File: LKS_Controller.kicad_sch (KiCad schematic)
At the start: 7 parts, among them J1 Conn_02x05_Odd_Even

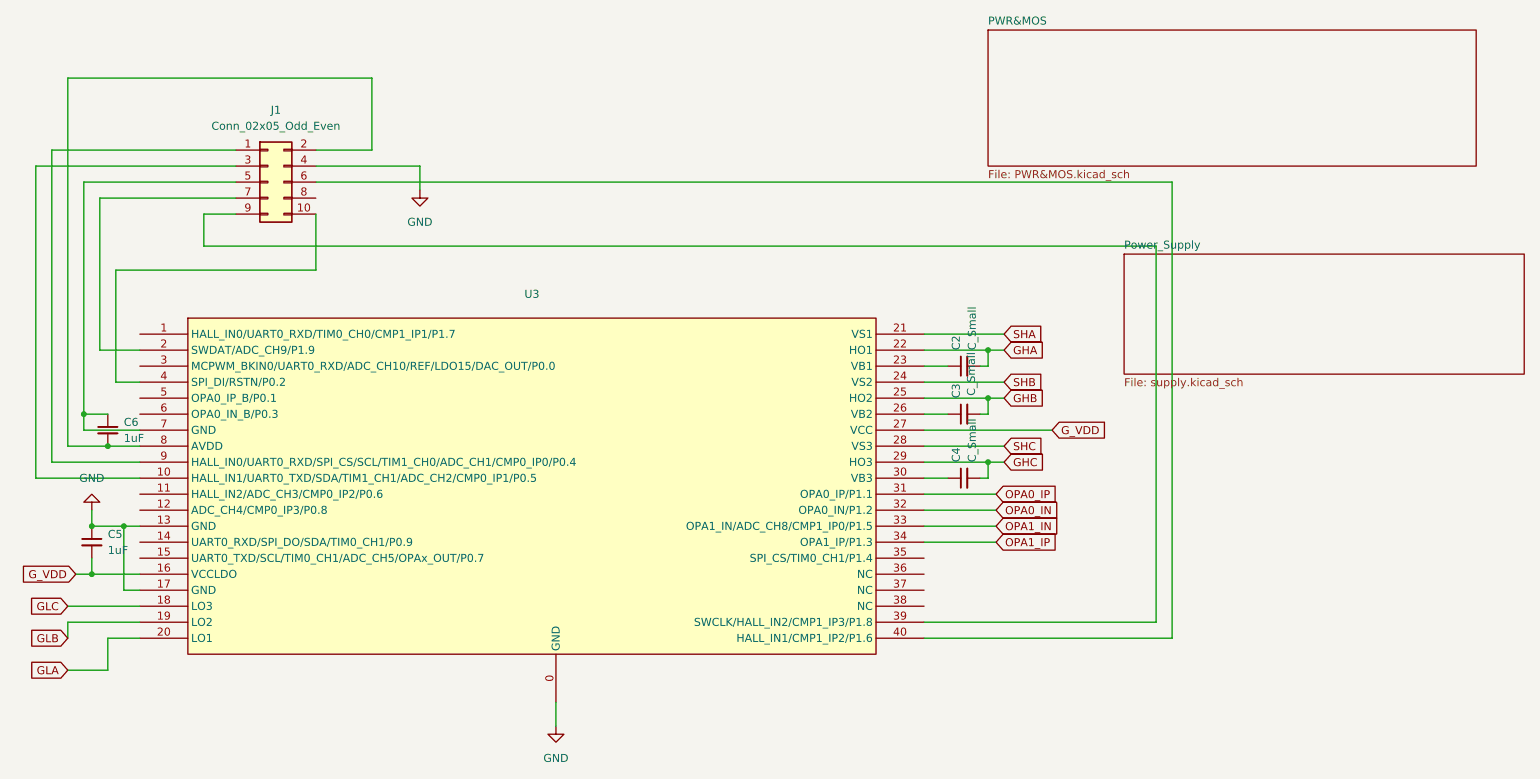
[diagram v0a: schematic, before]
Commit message: Fix ESC power, gate drive and current sensing schematics
Correct the buck converter and MCU symbols, bootstrap networks, MOSFET pulldowns and current sensing components. Migrate project libraries, synchronize PCB footprints and ground nets, and resolve ERC errors and warnings. Include LCSC BOMs and design notes; PCB routing remains incomplete.
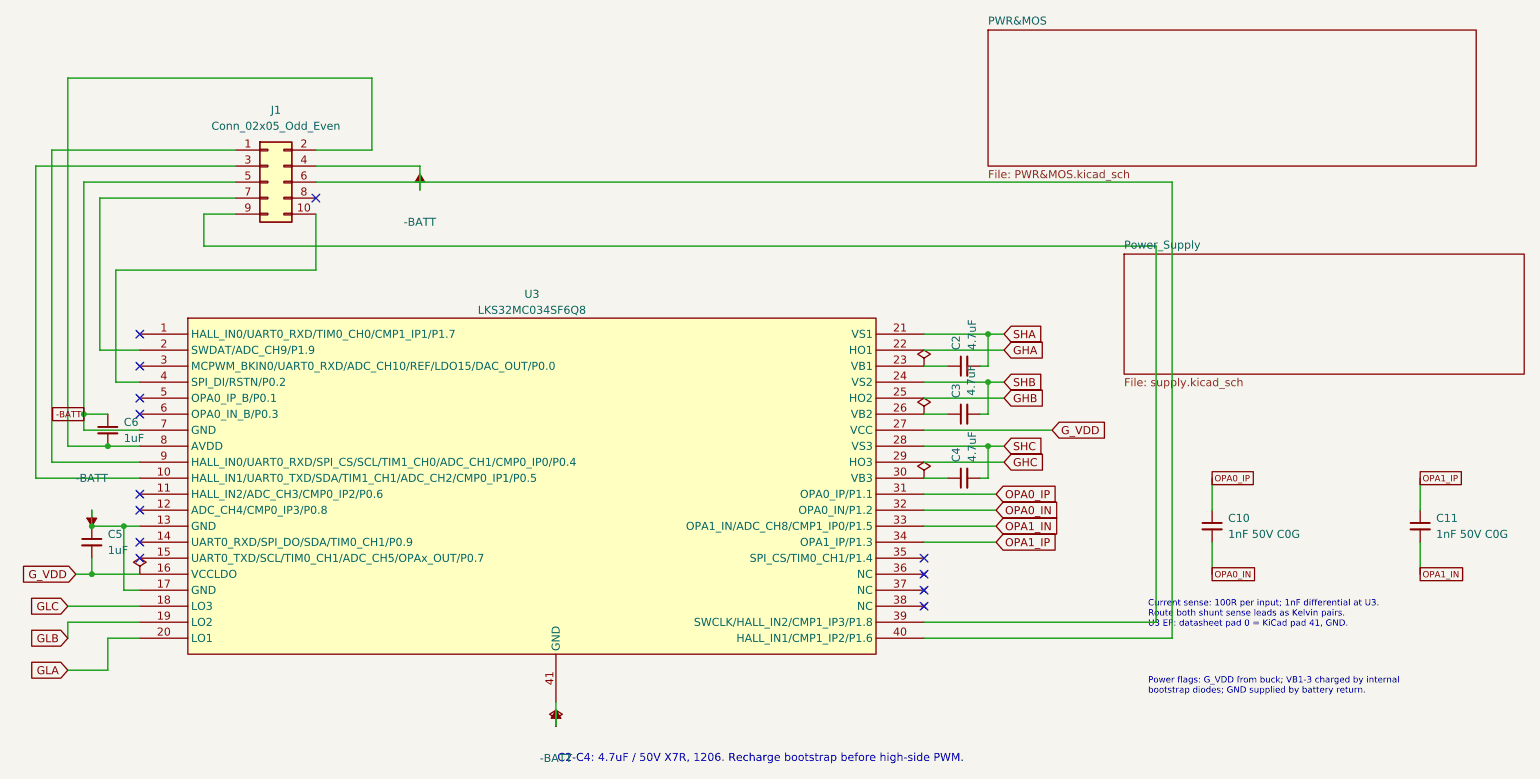
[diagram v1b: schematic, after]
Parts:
- added C10, C11: 1nF 50V C0G, Capacitor_SMD:C_0603_1608Metric_Pad1.08x0.95mm_HandSolder, symbol Device:C_Small
- C2, C3, C4: value C_Small -> 4.7uF; footprint Capacitor_SMD:C_0603_1608Metric_Pad1.08x0.95mm_HandSolder -> Capacitor_SMD:C_1206_3216Metric_Pad1.33x1.80mm_HandSolder; Dielectric (none) -> X7R; LCSC (none) -> C132170; MPN (none) -> CC1206KKX7R9BB475; Manufacturer (none) -> YAGEO; Tolerance (none) -> 10%; Voltage (none) -> 50V
- U3: value (none) -> LKS32MC034SF6Q8; symbol LINKOSEMI_LKS32MC034SF6M8:EVB_LKS034 -> Custom:LKS32MC034SF6Q8; LCSC (none) -> C19193083; MPN (none) -> LKS32MC034SF6Q8; Manufacturer (none) -> LINKOSEMI
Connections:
- net GHA: no longer C2.2
- net GHB: no longer C3.2
- net GHC: no longer C4.2
- net OPA0_IN: now also C10.2
- net OPA0_IP: now also C10.1
- net OPA1_IN: now also C11.2
- net OPA1_IP: now also C11.1
- net SHA: now also C2.2
- net SHB: now also C3.2
- net SHC: now also C4.2
- net -BATT: now reaches C6.1, J1.5 (Pin_5), U3.7 (GND)
- net -BATT: now also C5.1, J1.4 (Pin_4), U3.13 (GND), U3.17 (GND), U3.41 (GND)
- removed net GND: C5.1, J1.4 (Pin_4), U3.0 (GND), U3.13 (GND), U3.17 (GND)
- no-connect marks 0 -> 13
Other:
- note added: "C2-C4: 4.7uF / 50V X7R, 1206. Recharge bootstrap before high-side PWM."
- note added: "Current sense: 100R per input; 1nF differential at U3. Route both shunt sense leads as Kelvin pairs. U3 EP: datasheet pad 0 = KiCad pad 41, GND."
- note added: "Power flags: G_VDD from buck; VB1-3 charged by internal bootstrap diodes; GND supplied by battery return."
